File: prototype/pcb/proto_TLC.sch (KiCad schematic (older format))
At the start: 0 parts

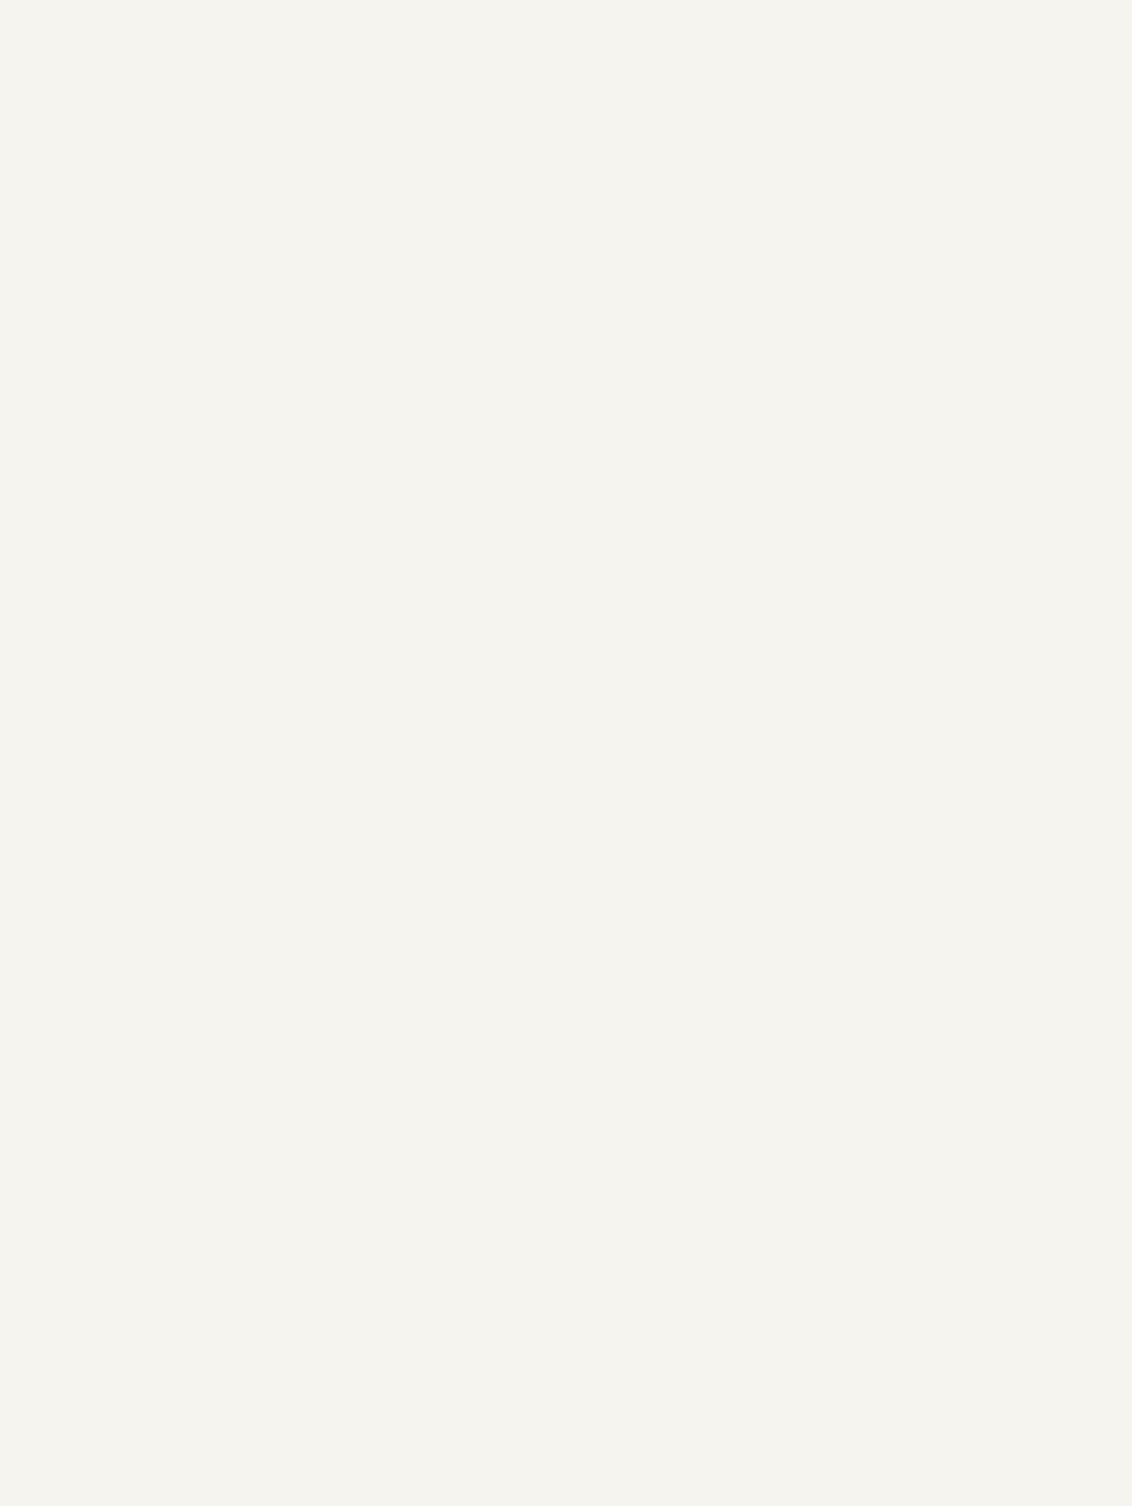
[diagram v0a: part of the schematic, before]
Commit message: Added leds to the schematic files
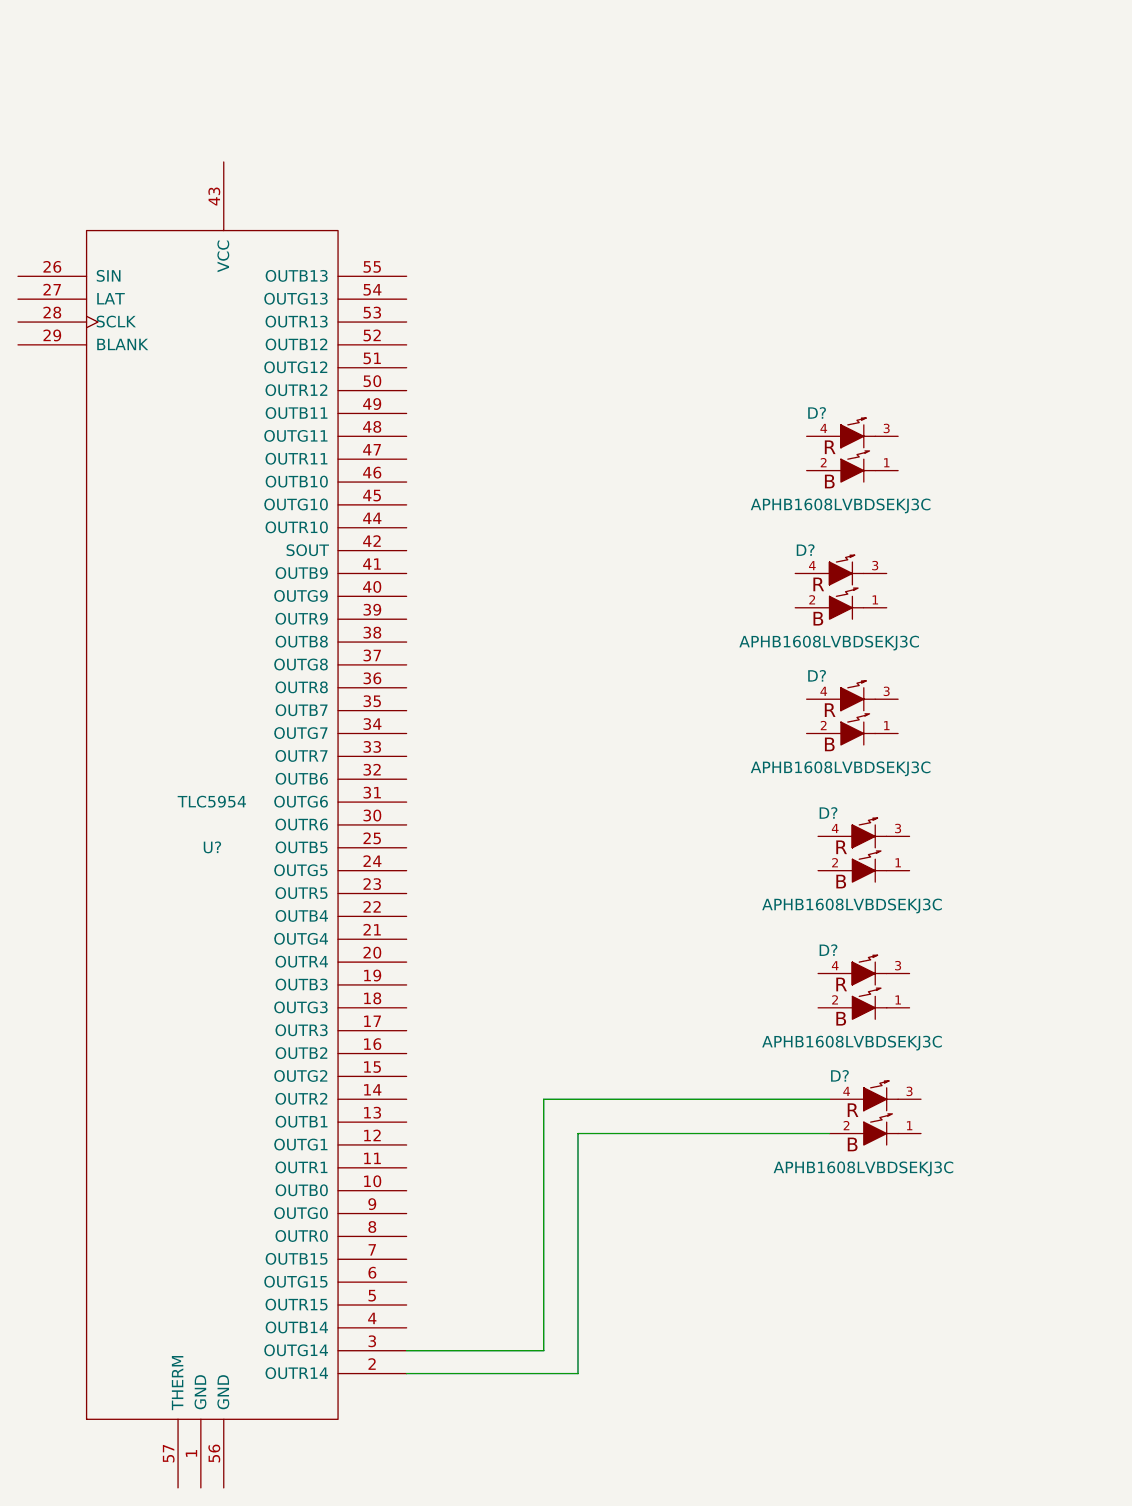
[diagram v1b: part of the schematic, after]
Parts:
- added D? (x6): APHB1608LVBDSEKJ3C, symbol APHB1608LVBDSEKJ3C
- added U?: TLC5954, MODULE, symbol TLC5954
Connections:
- new net: D?.2 (Blue+), U?.2 (OUTR14)
- new net: D?.4 (Red+), U?.3 (OUTG14)
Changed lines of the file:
@@
 LIBS:contrib
 LIBS:valves
+LIBS:TLC5954
+LIBS:watch_led
 LIBS:watch_proto_pcb-cache
 EELAYER 25 0
@@
 Text Notes 5150 1400 0    500  ~ 0
 TLC and LED Matric
+$Comp
+L TLC5954 U?
+U 1 1 574E1311
+P 5600 5600
+F 0 "U?" H 5600 5500 50  0000 C CNN
+F 1 "TLC5954" H 5600 5700 50  0000 C CNN
+F 2 "MODULE" H 5600 5600 50  0001 C CNN
+F 3 "DOCUMENTATION" H 5600 5600 50  0001 C CNN
+	1    5600 5600
+	1    0    0    -1
+$EndComp
+$Comp
+L APHB1608LVBDSEKJ3C D?
+U 1 1 574E238B
+P 8400 4000
+F 0 "D?" H 8200 4200 50  0000 L CNN
+F 1 "APHB1608LVBDSEKJ3C" H 8350 3800 50  0000 C CNN
+F 2 "" H 8400 3950 60  0000 C CNN
+F 3 "" H 8400 3950 60  0000 C CNN
+	1    8400 4000
+	1    0    0    -1
+$EndComp
+$Comp
+L APHB1608LVBDSEKJ3C D?
+U 1 1 574E23F2
+P 8350 4600
+F 0 "D?" H 8150 4800 50  0000 L CNN
+F 1 "APHB1608LVBDSEKJ3C" H 8300 4400 50  0000 C CNN
+F 2 "" H 8350 4550 60  0000 C CNN
+F 3 "" H 8350 4550 60  0000 C CNN
+	1    8350 4600
+	1    0    0    -1
+$EndComp
+$Comp
+L APHB1608LVBDSEKJ3C D?
+U 1 1 574E2426
+P 8400 5150
+F 0 "D?" H 8200 5350 50  0000 L CNN
+F 1 "APHB1608LVBDSEKJ3C" H 8350 4950 50  0000 C CNN
+F 2 "" H 8400 5100 60  0000 C CNN
+F 3 "" H 8400 5100 60  0000 C CNN
+	1    8400 5150
+	1    0    0    -1
+$EndComp
+$Comp
+L APHB1608LVBDSEKJ3C D?
+U 1 1 574E245C
+P 8450 5750
+F 0 "D?" H 8250 5950 50  0000 L CNN
+F 1 "APHB1608LVBDSEKJ3C" H 8400 5550 50  0000 C CNN
+F 2 "" H 8450 5700 60  0000 C CNN
+F 3 "" H 8450 5700 60  0000 C CNN
+	1    8450 5750
+	1    0    0    -1
+$EndComp
+$Comp
+L APHB1608LVBDSEKJ3C D?
+U 1 1 574E248E
+P 8450 6350
+F 0 "D?" H 8250 6550 50  0000 L CNN
+F 1 "APHB1608LVBDSEKJ3C" H 8400 6150 50  0000 C CNN
+F 2 "" H 8450 6300 60  0000 C CNN
+F 3 "" H 8450 6300 60  0000 C CNN
+	1    8450 6350
+	1    0    0    -1
+$EndComp
+$Comp
+L APHB1608LVBDSEKJ3C D?
+U 1 1 574E24C0
+P 8500 6900
+F 0 "D?" H 8300 7100 50  0000 L CNN
+F 1 "APHB1608LVBDSEKJ3C" H 8450 6700 50  0000 C CNN
+F 2 "" H 8500 6850 60  0000 C CNN
+F 3 "" H 8500 6850 60  0000 C CNN
+	1    8500 6900
+	1    0    0    -1
+$EndComp
+Wire Wire Line
+	6450 8000 7200 8000
+Wire Wire Line
+	7200 8000 7200 6950
+Wire Wire Line
+	7200 6950 8300 6950
+Wire Wire Line
+	6450 7900 7050 7900
+Wire Wire Line
+	7050 7900 7050 6800
+Wire Wire Line
+	7050 6800 8300 6800
 $EndSCHEMATC

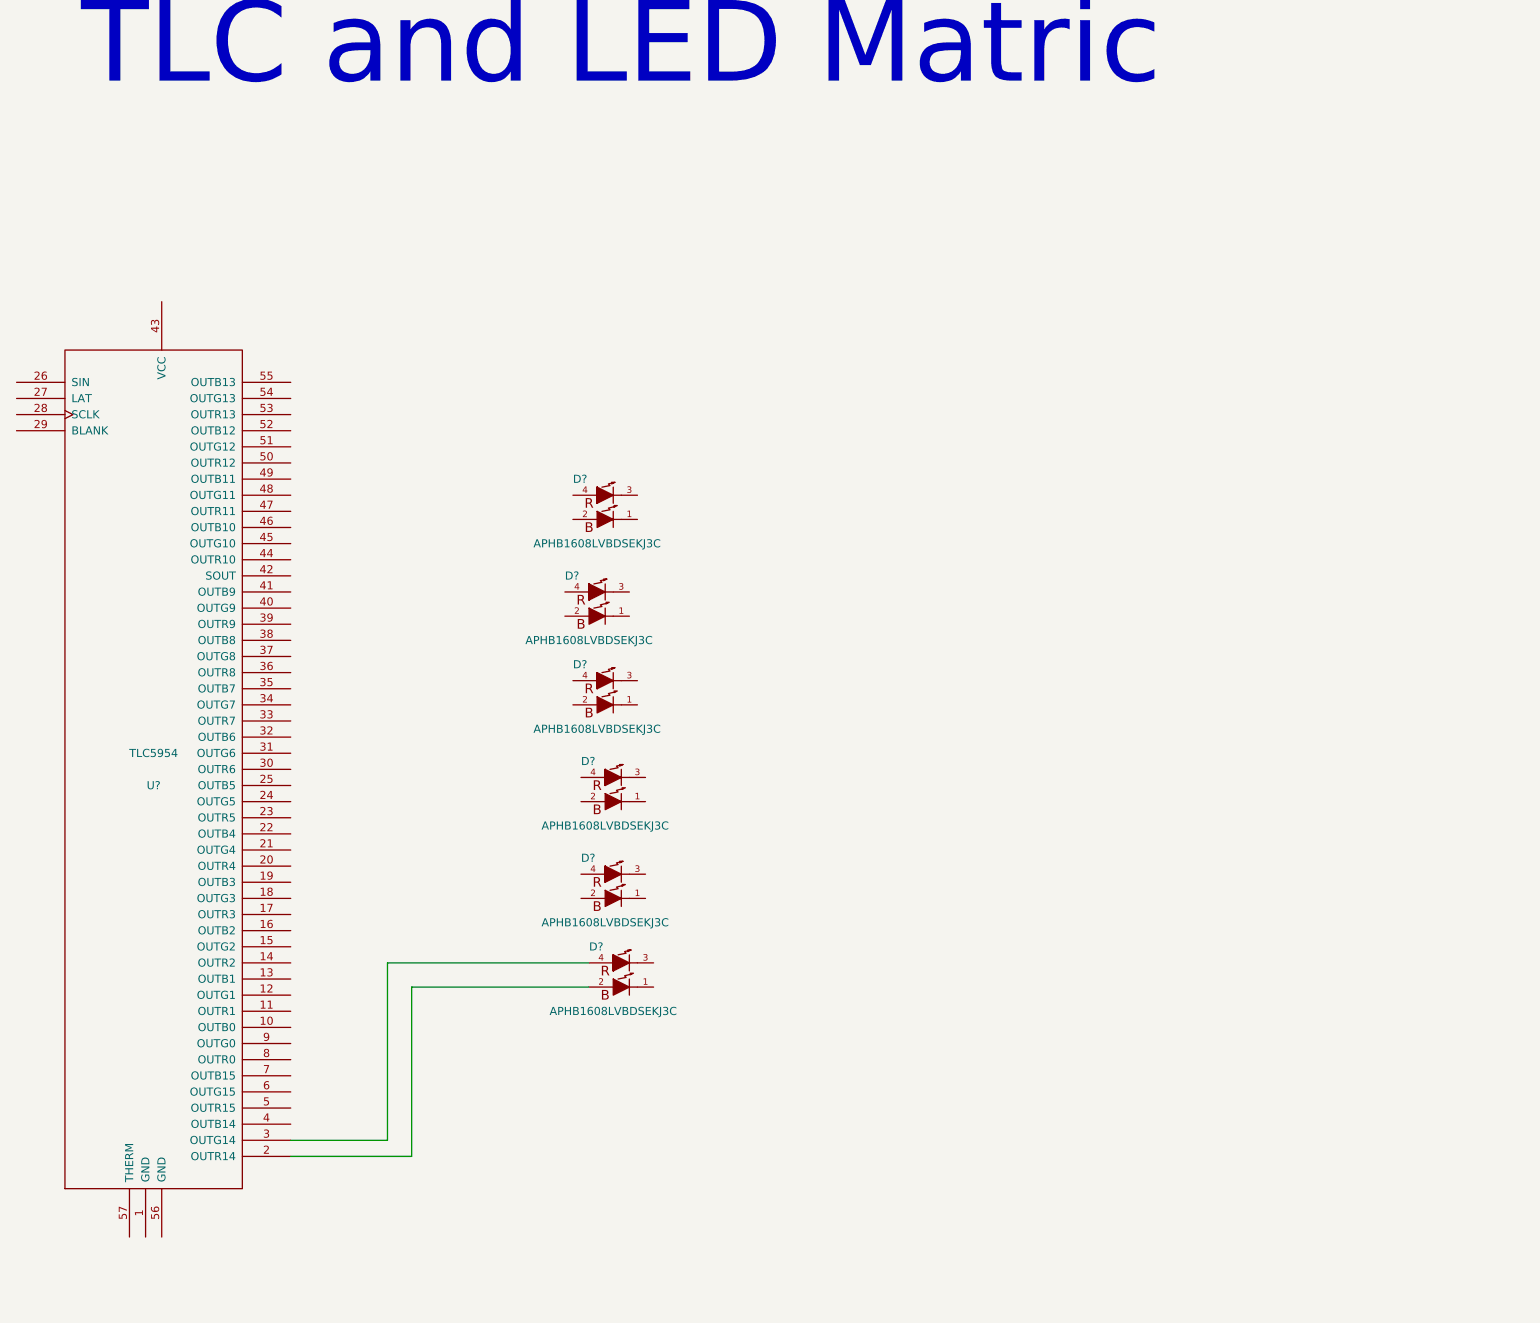
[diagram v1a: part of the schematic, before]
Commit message: Added TLC, LEDs, and bus lines
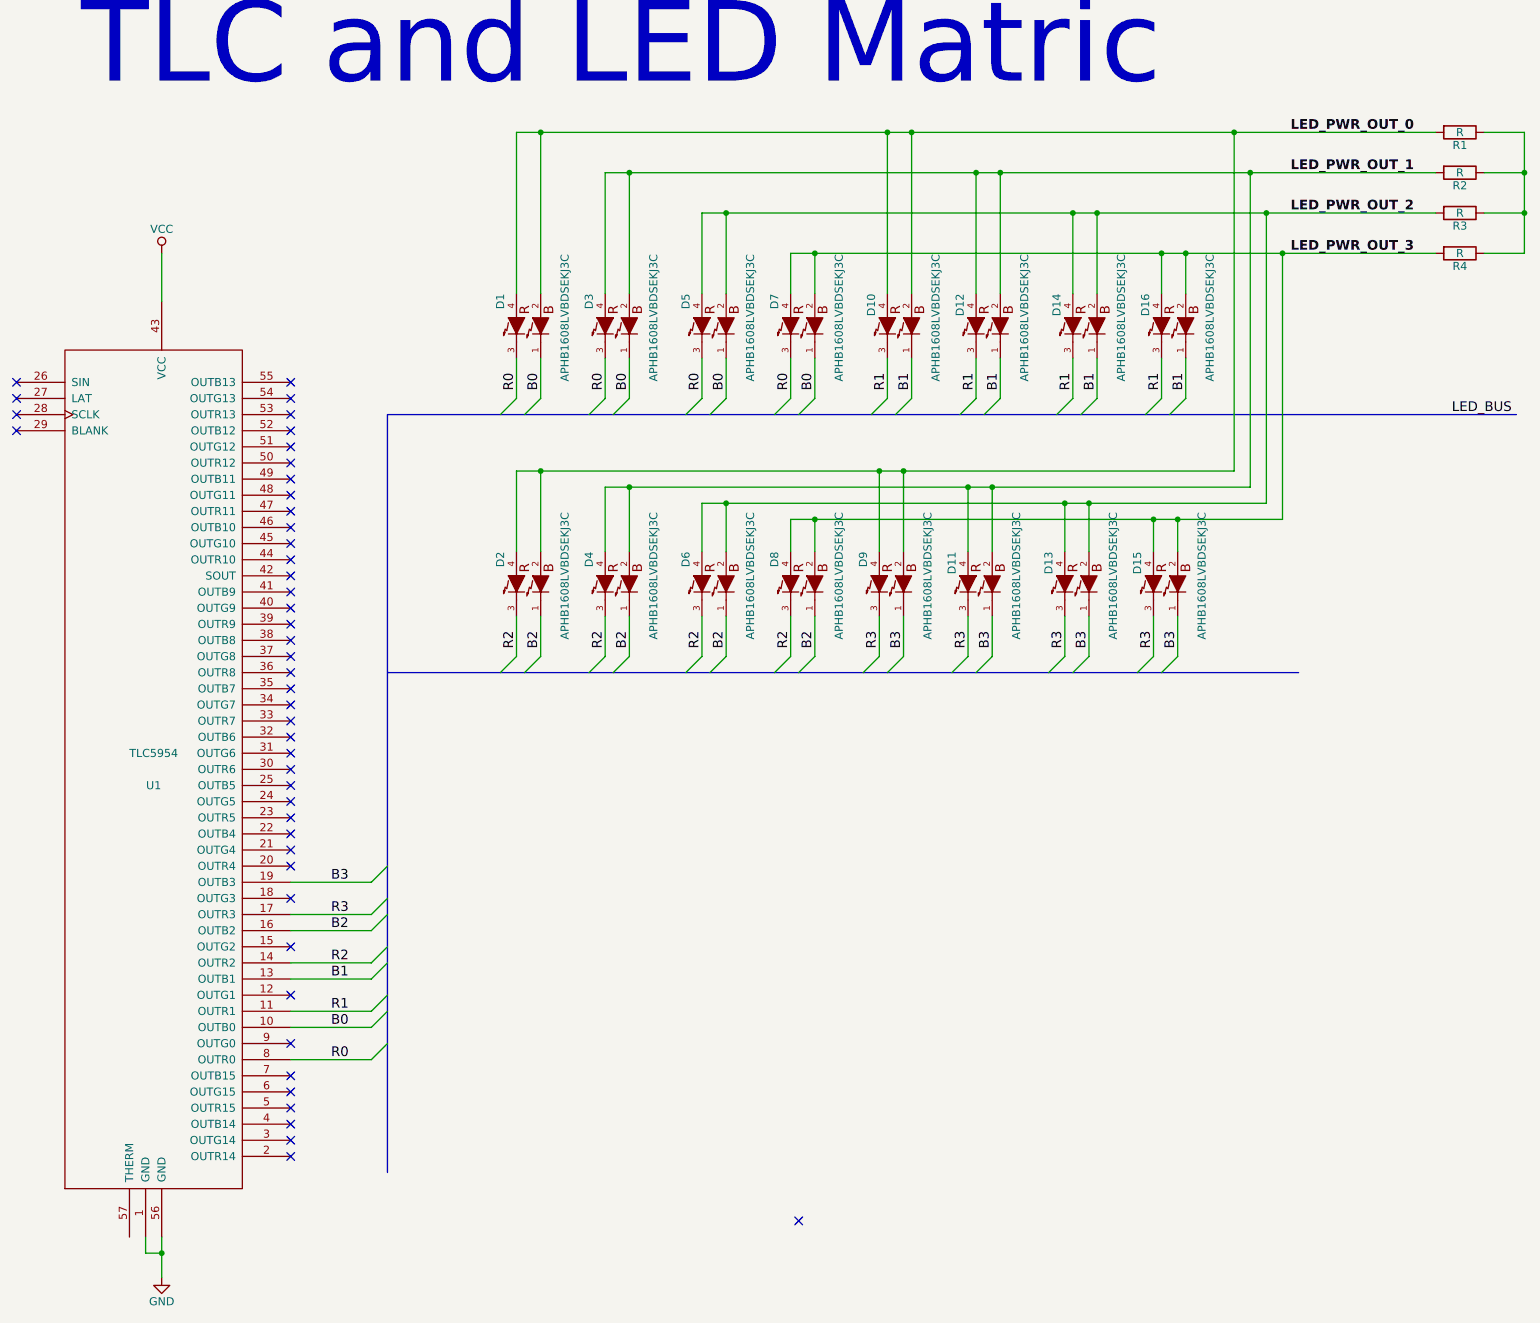
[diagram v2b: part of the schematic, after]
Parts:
- added D11, D13, D14, D15, D16, D2, D4, D6, D8, D9: APHB1608LVBDSEKJ3C, symbol APHB1608LVBDSEKJ3C
- added R1, R2, R3, R4: R, symbol R
- gave numbers to parts that had none: 7
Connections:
- net GND: now reaches U1.1 (GND)
- net GND: now also U1.56 (GND)
- net B0: now reaches U1.10 (OUTB0)
- net B0: now also D1.1 (Blue-), D3.1 (Blue-), D5.1 (Blue-), D7.1 (Blue-)
- net R1: now reaches U1.11 (OUTR1)
- net R1: now also D10.3 (Red-), D12.3 (Red-), D14.3 (Red-), D16.3 (Red-)
- net B1: now reaches U1.13 (OUTB1)
- net B1: now also D10.1 (Blue-), D12.1 (Blue-), D14.1 (Blue-), D16.1 (Blue-)
- net R2: now reaches U1.14 (OUTR2)
- net R2: now also D2.3 (Red-), D4.3 (Red-), D6.3 (Red-), D8.3 (Red-)
- net B2: now reaches U1.16 (OUTB2)
- net B2: now also D2.1 (Blue-), D4.1 (Blue-), D6.1 (Blue-), D8.1 (Blue-)
- net R3: now reaches U1.17 (OUTR3)
- net R3: now also D11.3 (Red-), D13.3 (Red-), D15.3 (Red-), D9.3 (Red-)
- net B3: now reaches U1.19 (OUTB3)
- net B3: now also D11.1 (Blue-), D13.1 (Blue-), D15.1 (Blue-), D9.1 (Blue-)
- net at U1.2 (OUTR14): no longer D12.2 (Blue+)
- net at U1.3 (OUTG14): no longer D12.4 (Red+)
- net VCC: now reaches U1.43 (VCC)
- net R0: now reaches U1.8 (OUTR0)
- net R0: now also D1.3 (Red-), D3.3 (Red-), D5.3 (Red-), D7.3 (Red-)
- net LED_PWR_OUT_0: now reaches D1.2 (Blue+)
- net LED_PWR_OUT_0: now also D1.4 (Red+), D10.2 (Blue+), D10.4 (Red+), D2.2 (Blue+), D2.4 (Red+), D9.2 (Blue+), D9.4 (Red+), R1.2
- net LED_PWR_OUT_1: now reaches D3.2 (Blue+)
- net LED_PWR_OUT_1: now also D12.2 (Blue+), D12.4 (Red+), D3.4 (Red+), D11.2 (Blue+), D11.4 (Red+), D4.2 (Blue+), D4.4 (Red+), R2.2
- net LED_PWR_OUT_2: now reaches D5.2 (Blue+)
- net LED_PWR_OUT_2: now also D5.4 (Red+), D13.2 (Blue+), D13.4 (Red+), D14.2 (Blue+), D14.4 (Red+), D6.2 (Blue+), D6.4 (Red+), R3.2
- net LED_PWR_OUT_3: now reaches D7.2 (Blue+)
- net LED_PWR_OUT_3: now also D7.4 (Red+), D15.2 (Blue+), D15.4 (Red+), D16.2 (Blue+), D16.4 (Red+), D8.2 (Blue+), D8.4 (Red+), R4.2
- new net: R1.1, R2.1, R3.1, R4.1
- no-connect marks 0 -> 46
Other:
- moved on the sheet: D1, D10, D12, D3, D5, D7
